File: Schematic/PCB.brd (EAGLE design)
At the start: 100 x 80 mm, 68 parts, among them J1 POWER_JACK, U1 V_REG_317SINK

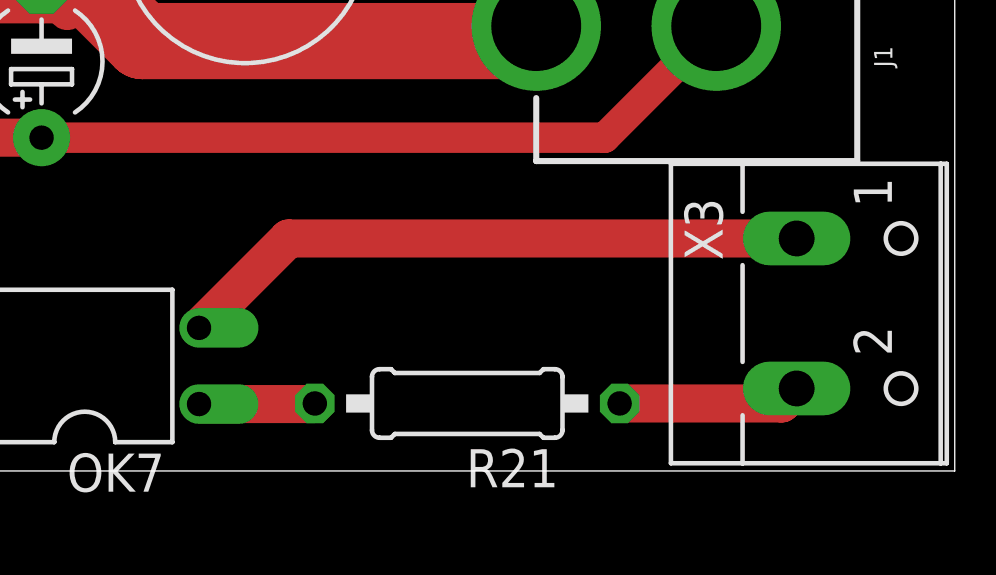
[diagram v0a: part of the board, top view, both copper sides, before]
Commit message: added protection diode on zero cross detector
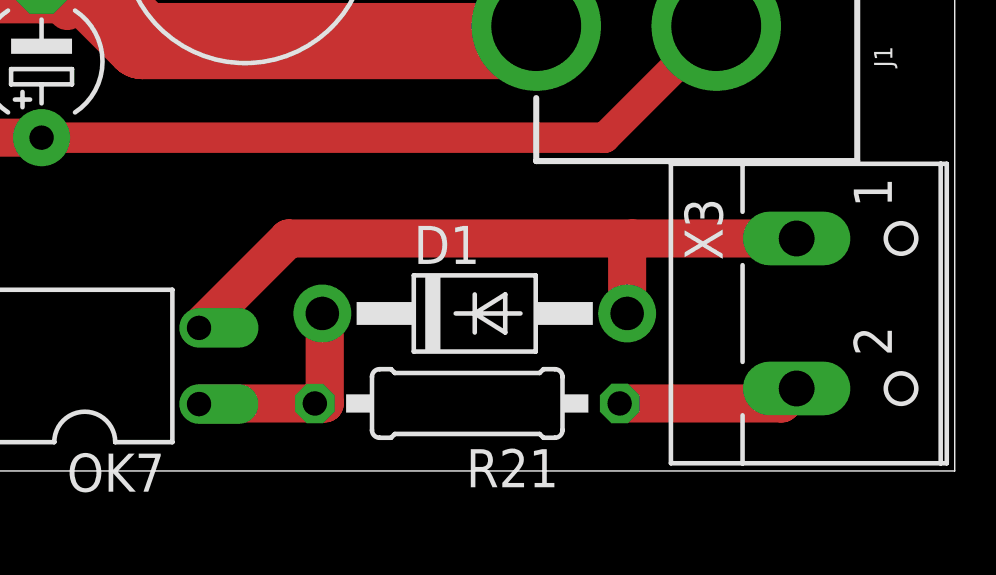
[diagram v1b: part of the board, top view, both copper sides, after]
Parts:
- added D1: 1N4004, adafruit:DO41-10
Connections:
- net LINE_COM: now also D1.A
- net N$14: now also D1.C
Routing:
- net N$14: track 3.87 -> 7.40 mm
- net LINE_COM: track 21.2 -> 23.7 mm
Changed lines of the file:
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@@
 <attribute name="VALUE" x="87" y="19.543" size="0.6096" layer="28" font="vector" ratio="20" rot="MR0" align="top-center"/>
+</element>
+<element name="D1" library="adafruit" library_urn="urn:adsk.eagle:library:420" package="DO41-10" package3d_urn="urn:adsk.eagle:package:6240344/1" value="1N4004" x="84" y="5.25" smashed="yes">
+<attribute name="NAME" x="81.968" y="6.901" size="1.27" layer="25" ratio="10"/>
+<attribute name="VALUE" x="81.968" y="2.456" size="1.27" layer="27" ratio="10"/>
 </element>
 </elements>
@@
 <wire x1="94.23" y1="2.25" x2="88.83" y2="2.25" width="1.27" layer="1"/>
 </signal>
-<signal name="N$14">
-<contactref element="R21" pad="2"/>
-<contactref element="OK7" pad="1"/>
-<wire x1="78.67" y1="2.25" x2="78.65" y2="2.23" width="1.27" layer="1"/>
-<wire x1="78.65" y1="2.23" x2="74.81" y2="2.23" width="1.27" layer="1"/>
-</signal>
 <signal name="LINE_COM">
 <contactref element="OK7" pad="2"/>
 <contactref element="X3" pad="1"/>
 <wire x1="74.81" y1="4.77" x2="77.79" y2="7.75" width="1.27" layer="1"/>
-<wire x1="77.79" y1="7.75" x2="94.73" y2="7.75" width="1.27" layer="1"/>
+<wire x1="77.79" y1="7.75" x2="89.25" y2="7.75" width="1.27" layer="1"/>
+<contactref element="D1" pad="A"/>
+<wire x1="89.25" y1="7.75" x2="94.73" y2="7.75" width="1.27" layer="1"/>
+<wire x1="89.08" y1="5.25" x2="89.08" y2="7.58" width="1.27" layer="1"/>
+<wire x1="89.08" y1="7.58" x2="89.25" y2="7.75" width="0.1524" layer="1"/>
 </signal>
 <signal name="ZERO_CROSS_PULSE">
@@
 <wire x1="3.9" y1="42" x2="3.81" y2="41.91" width="0" layer="19" extent="1-1"/>
 </signal>
+<signal name="N$14">
+<contactref element="R21" pad="2"/>
+<contactref element="OK7" pad="1"/>
+<contactref element="D1" pad="C"/>
+<wire x1="78.67" y1="2.25" x2="78.5" y2="2.25" width="0.1524" layer="1"/>
+<wire x1="79" y1="2.25" x2="78.5" y2="2.25" width="1.27" layer="1"/>
+<wire x1="78.5" y1="2.25" x2="74.83" y2="2.25" width="1.27" layer="1"/>
+<wire x1="74.83" y1="2.25" x2="74.81" y2="2.23" width="0.1524" layer="1"/>
+<wire x1="78.92" y1="5.25" x2="79" y2="5.17" width="1.27" layer="1"/>
+<wire x1="79" y1="5.17" x2="79" y2="2.25" width="1.27" layer="1"/>
+</signal>
 </signals>

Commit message: finished PCB and corrected schematic
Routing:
- net 15VDC: track 104.4 -> 135.6 mm, vias 2 -> 5
- net GND: track 303.3 -> 305.2 mm
- net PHASE_+: track 46.6 -> 48.4 mm
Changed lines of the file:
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@@
 <wire x1="57.903" y1="66.44" x2="57.093" y2="67.25" width="0.8128" layer="1"/>
 <wire x1="58.56" y1="66.44" x2="57.903" y2="66.44" width="0.8128" layer="1"/>
-<wire x1="62.66" y1="62.34" x2="58.56" y2="66.44" width="0.8128" layer="1"/>
 <wire x1="43.5" y1="69" x2="45.25" y2="67.25" width="0.8128" layer="1"/>
 <wire x1="45.25" y1="67.25" x2="56.25" y2="67.25" width="0.8128" layer="1"/>
@@
 <wire x1="40.64" y1="48.26" x2="42.74" y2="48.26" width="1.27" layer="1"/>
 <wire x1="42.74" y1="48.26" x2="43.5" y2="47.5" width="1.27" layer="1"/>
-<wire x1="43.5" y1="47.5" x2="45.5" y2="47.5" width="1.27" layer="1"/>
+<wire x1="43.5" y1="47.5" x2="44.5" y2="48.5" width="1.27" layer="1"/>
+<wire x1="44.5" y1="48.5" x2="45.5" y2="47.5" width="1.27" layer="1"/>
 <wire x1="40.64" y1="26.67" x2="43.42" y2="26.67" width="1.27" layer="1"/>
 <wire x1="43.42" y1="26.67" x2="43.5" y2="26.75" width="1.27" layer="1"/>
@@
 <wire x1="61.61" y1="44.41" x2="60.2" y2="43" width="1.016" layer="1"/>
 <contactref element="C10" pad="-"/>
-<wire x1="62.66" y1="62.34" x2="63.04" y2="62.34" width="0" layer="19" extent="1-1"/>
+<wire x1="57.903" y1="66.44" x2="58.94" y2="66.44" width="0.8128" layer="1"/>
+<wire x1="58.94" y1="66.44" x2="63.04" y2="62.34" width="0.8128" layer="1"/>
 </signal>
 <signal name="3V3_SUPPLY_1">
@@
 <contactref element="U$2" pad="3"/>
 <wire x1="70.16" y1="40.485" x2="72.5" y2="38.145" width="1.016" layer="1"/>
-<wire x1="72.5" y1="38.145" x2="72.5" y2="28.75" width="1.016" layer="1"/>
+<wire x1="72.5" y1="38.145" x2="72.5" y2="32.5" width="1.016" layer="1"/>
 <contactref element="C12" pad="+"/>
+<wire x1="72.5" y1="32.5" x2="72.5" y2="28.75" width="1.016" layer="1"/>
 <wire x1="72.5" y1="28.75" x2="72.5" y2="26.73" width="1.016" layer="1"/>
 <wire x1="72.5" y1="26.73" x2="71.26" y2="25.49" width="1.016" layer="1"/>
@@
 <wire x1="71.75" y1="28" x2="69" y2="28" width="1.016" layer="1"/>
 <via x="69" y="28" extent="1-16" drill="0.35"/>
+<via x="66.5" y="11.11" extent="1-16" drill="0.35"/>
 <wire x1="69" y1="28" x2="66.5" y2="25.5" width="1.016" layer="16"/>
-<via x="66.5" y="11.11" extent="1-16" drill="0.35"/>
 <wire x1="66.5" y1="25.5" x2="66.5" y2="11.11" width="1.016" layer="16"/>
 <contactref element="U$2" pad="8"/>
@@
 <contactref element="C10" pad="+"/>
 <wire x1="65.76" y1="57.26" x2="64.75" y2="57.26" width="0.8128" layer="1"/>
+<wire x1="64.75" y1="55.75" x2="64.75" y2="57.26" width="0.8128" layer="1"/>
+<via x="64.75" y="55.75" extent="1-16" drill="0.35"/>
+<via x="64.75" y="49.49" extent="1-16" drill="0.35"/>
+<wire x1="64.75" y1="55.75" x2="64.75" y2="49.49" width="0.8128" layer="16"/>
+<wire x1="64.75" y1="49.49" x2="64.75" y2="34.75" width="0.8128" layer="16"/>
+<wire x1="67" y1="32.5" x2="72.5" y2="32.5" width="0.8128" layer="16"/>
+<via x="72.5" y="32.5" extent="1-16" drill="0.35"/>
+<wire x1="64.75" y1="34.75" x2="67" y2="32.5" width="0.8128" layer="16"/>
 <wire x1="64.75" y1="57.26" x2="63.04" y2="57.26" width="0.8128" layer="1"/>
-<wire x1="64.75" y1="57.26" x2="64.75" y2="49.49" width="0" layer="19" extent="1-1"/>
-<wire x1="64.75" y1="49.49" x2="70.16" y2="40.485" width="0" layer="19" extent="1-1"/>
 </signal>
 <signal name="R_L_PWM_ISOLATED">
@@
 <wire x1="24.9894" y1="8.7606" x2="27.2512" y2="8.7606" width="0.8128" layer="1"/>
 <wire x1="15.5" y1="22.33" x2="11" y2="26.83" width="0.8128" layer="1"/>
-<wire x1="11" y1="36.5" x2="5.5" y2="42" width="0.8128" layer="1"/>
+<wire x1="11" y1="36.5" x2="6.25" y2="41.25" width="0.8128" layer="1"/>
+<wire x1="6.25" y1="41.25" x2="5.5" y2="42" width="0.8128" layer="1"/>
 <wire x1="5.5" y1="42" x2="3.9" y2="42" width="0.8128" layer="1"/>
 <wire x1="11" y1="26.83" x2="11" y2="36.5" width="0.8128" layer="1"/>
-<wire x1="3.9" y1="42" x2="3.81" y2="41.91" width="0" layer="19" extent="1-1"/>
+<wire x1="3.81" y1="41.91" x2="3.9" y2="42" width="0.8128" layer="1"/>
+<wire x1="3.9" y1="42" x2="5.5" y2="42" width="0.8128" layer="1"/>
 </signal>
 <signal name="N$14">
@@
 <mfgpreviewcolor name="substratecolor" color="0xFF786E46"/>
 </mfgpreviewcolors>
+<errors>
+</errors>
 </board>
 </drawing>
